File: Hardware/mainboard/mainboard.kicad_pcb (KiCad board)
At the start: 4 copper layers, 78 x 69.1 mm, 45 parts, among them J1 559592430, J2 status LEDs 1, J3 status LEDs 2, J4 B05B-XASK-1LFSN, J5 race start, J6 usb-ttl, J7 jtag, J8 KUSBX-SMT-CS-6-BTR, SW1 ON-BOARD, SW2 BOT Switch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

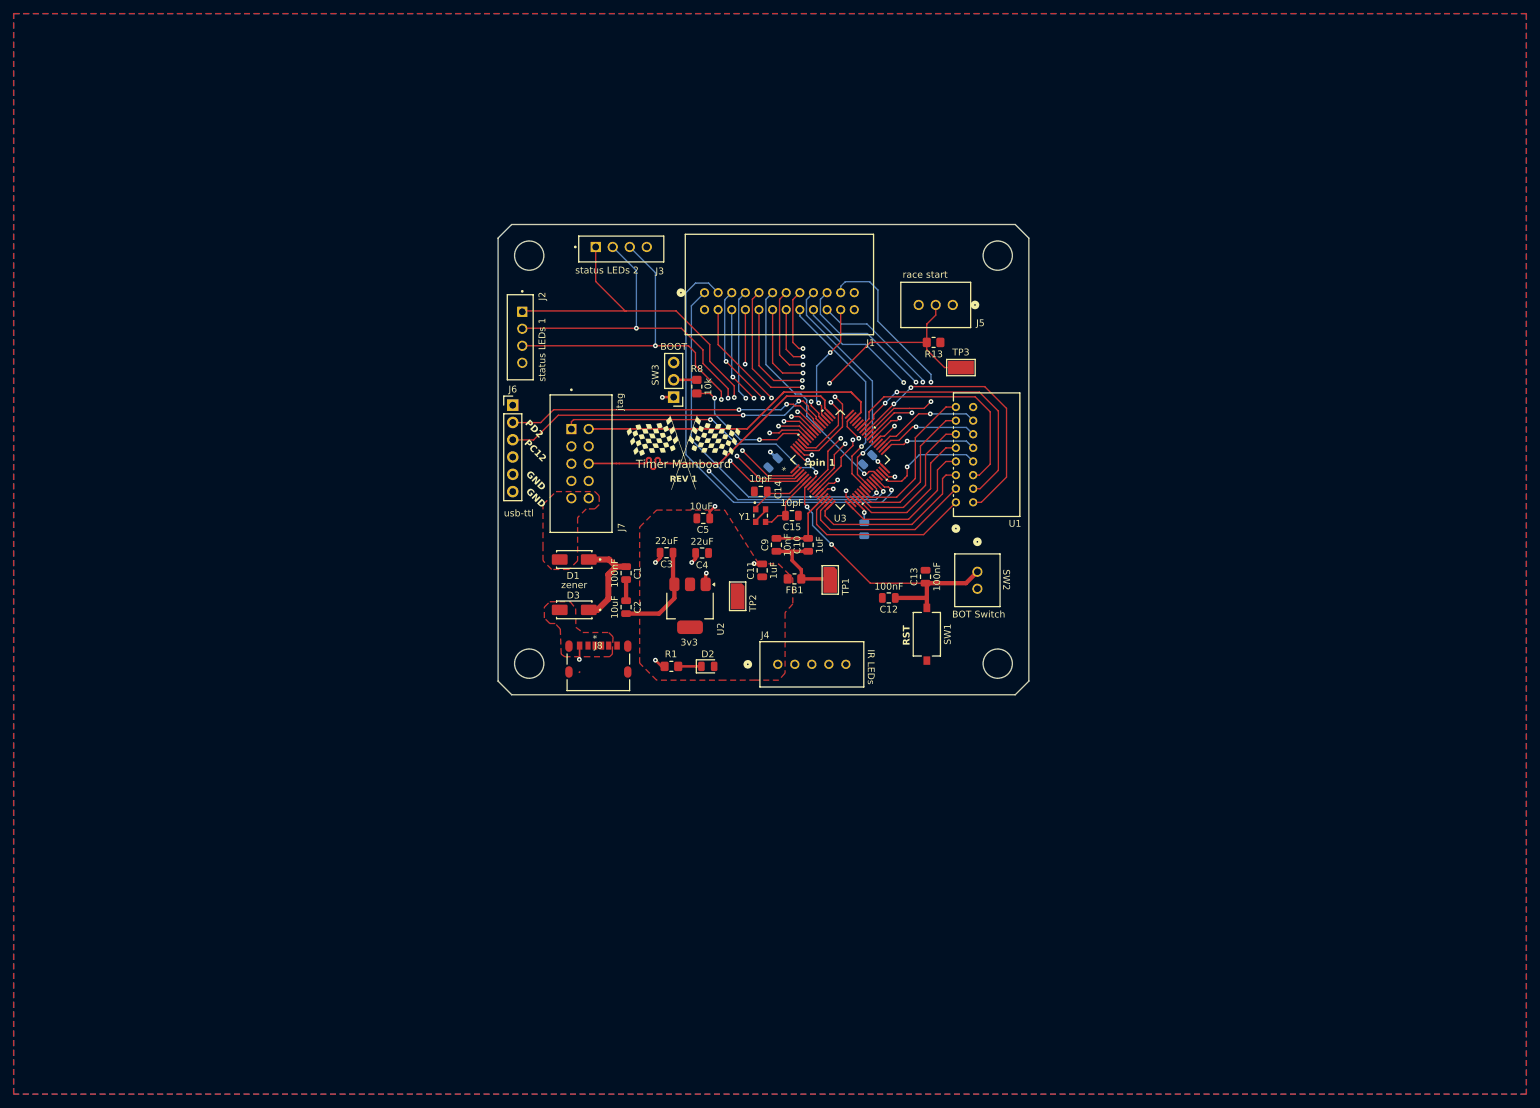
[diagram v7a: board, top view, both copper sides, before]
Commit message: fixed schematic pcb agreement errors
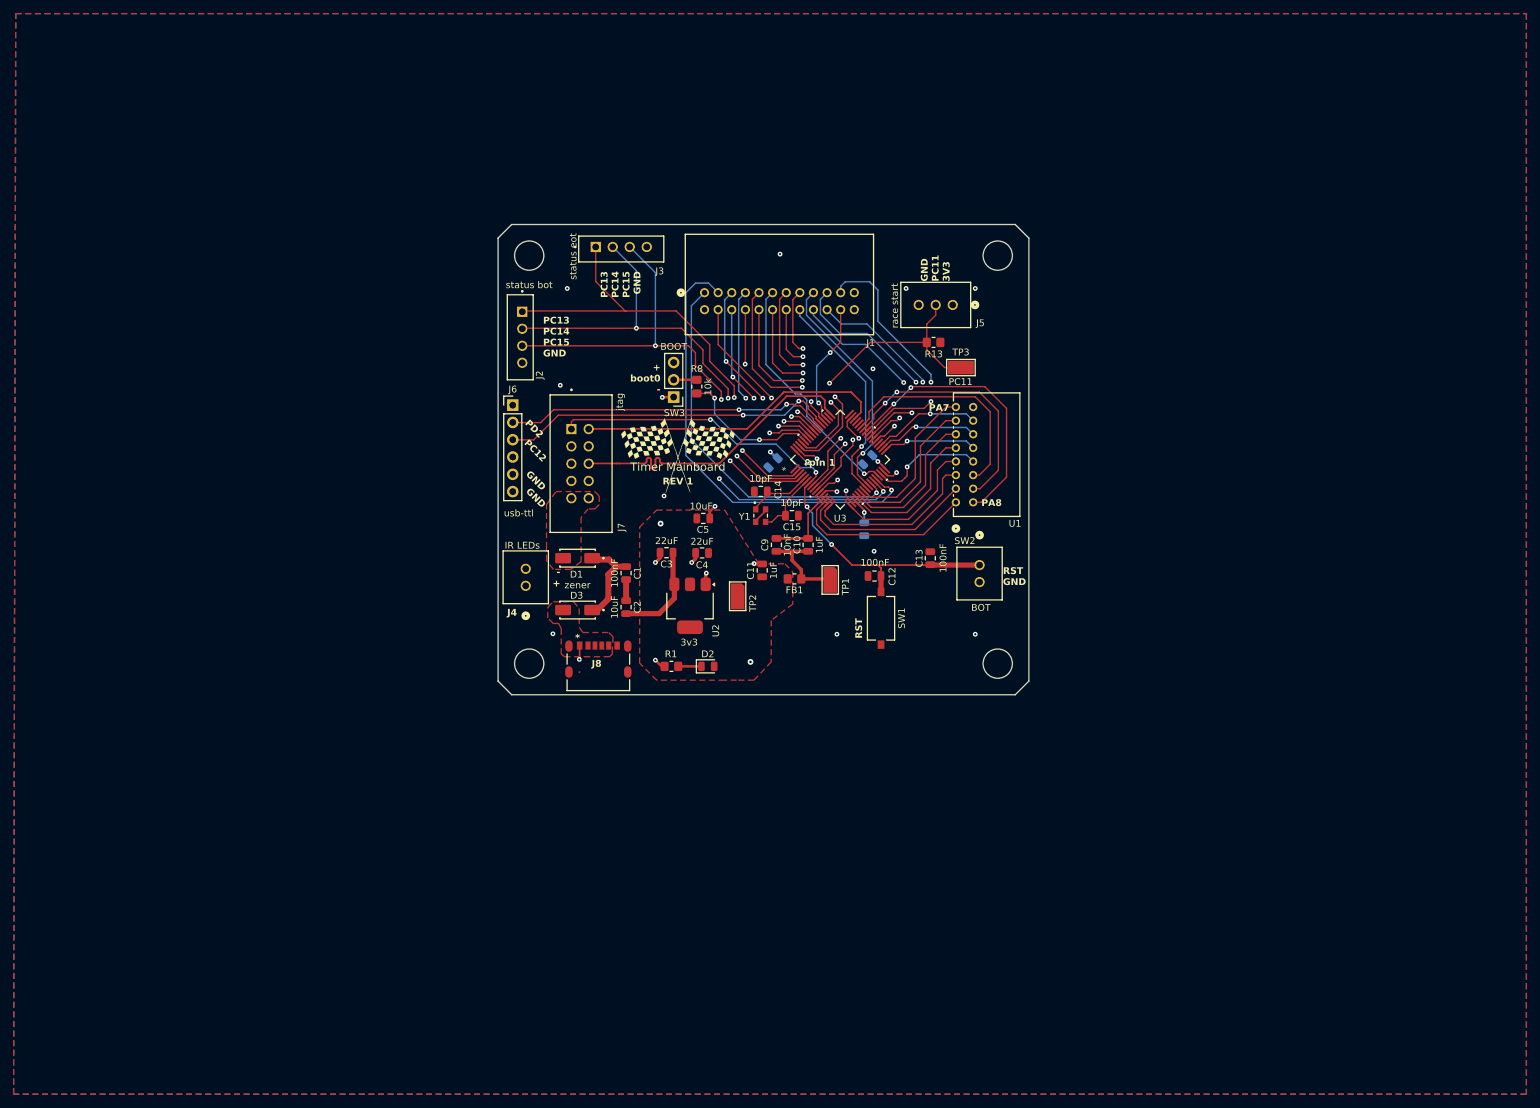
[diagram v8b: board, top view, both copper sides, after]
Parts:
- removed REF** (x4): MountingHole_4.3mm_M4, MountingHole:MountingHole_4.3mm_M4
- added H1: MountingHole, MountingHole:MountingHole_4.3mm_M4_DIN965, F.Cu at (66.5, 25.7)
- added H2: MountingHole, MountingHole:MountingHole_4.3mm_M4_DIN965, F.Cu at (135.4, 25.7)
- added H3: MountingHole, MountingHole:MountingHole_4.3mm_M4_DIN965, F.Cu at (66.5, 85.6)
- added H4: MountingHole, MountingHole:MountingHole_4.3mm_M4_DIN965, F.Cu at (135.4, 85.6)
- J2: value status LEDs 1 -> status bot
- J3: value status LEDs 2 -> status eot
- J4: value B05B-XASK-1LFSN -> B02B-XASK-1LFSN; footprint 1X05_JST:1x05_jst -> BIG LIBRARY:1X02_JST
- SW2: value BOT Switch -> BOT
- TP3: value TestPoint -> PC11
- moved J4 38.8 mm to (66.0, 74.2), turned to 90 degrees
- moved SW1 7.13 mm to (118.2, 78.9)
- moved C12 3.84 mm to (117.3, 72.7)
- moved C13 2.81 mm to (125.5, 70.1)
- moved SW2 1.03 mm to (132.7, 71.1)
- moved G*** 0.91 mm to (88.4, 55.0)
- moved D1 0.53 mm to (73.7, 70.1)
- moved D3 0.50 mm to (73.7, 77.7)
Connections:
- J4 pad 2: IR_1 -> GND
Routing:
- net RST: track 86.2 -> 80.6 mm
- net GND: track 26.6 -> 28.4 mm, vias 13 -> 24
- net +3.3V: vias 4 -> 6
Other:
- board text added: "+ -"
- board text added: "+ boot0 -"
- board text added: "GND PC11 3V3"
- board text added: "PA7"
- board text added: "PA8"
- board text added: "PC13 PC14 PC15 GND"
- board text added: "RST GND"
